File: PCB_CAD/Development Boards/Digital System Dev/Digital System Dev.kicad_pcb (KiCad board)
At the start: 6 copper layers, 100 x 100 mm, 189 parts, among them J1 STLINK, J10 F2_LOGIC, J101 Conn_01x04_Socket, J102 Conn_01x04_Socket, J103 Conn_01x04_Socket, J104 Conn_01x04_Socket, J13 F3_LOGIC, J15 DC_10V, J17 DISP0, J18 DISP1, J19 DISP2, J2 FADER_POW, J20 DISP3, J24 I2C_SEL_CLK, J25 I2C_SEL_SDA, J26 CV_SW_1, J27 CV_SW_2, J28 CV_SW_4, J29 CV_SW_3, J3 F0_LOGIC, J30 I2C, J31 CTRL_POW_SR, J4 FADER_POS, J5 LED_SEL, J6 F1_LOGIC, J7 SPI_MASTER, J8 EXT_POW_IN, Q1 2N7002, SW1 RESET, SW101 B2A, SW102 B2B, SW103 B2C, SW104 K1A, SW105 K1B, U1 STM32G474VETx, U101 74HCT595, U102 MCP23017x-x-SS, U28 74HC595, U29 74HC595, U30 74HC595, U31 74HC595, U32 74HC595, U33 74HC595, U34 74HC595, U35 74HC595, U36 74HC595, U37 74HC595, U38 74HC595, U39 74HC595, U4 TPS54302DDCT, U4 TPS5430DDA, U5 MCP4728, U6 TPS54302DDCT, U6 TPS5430DDA, X1 HSE_24

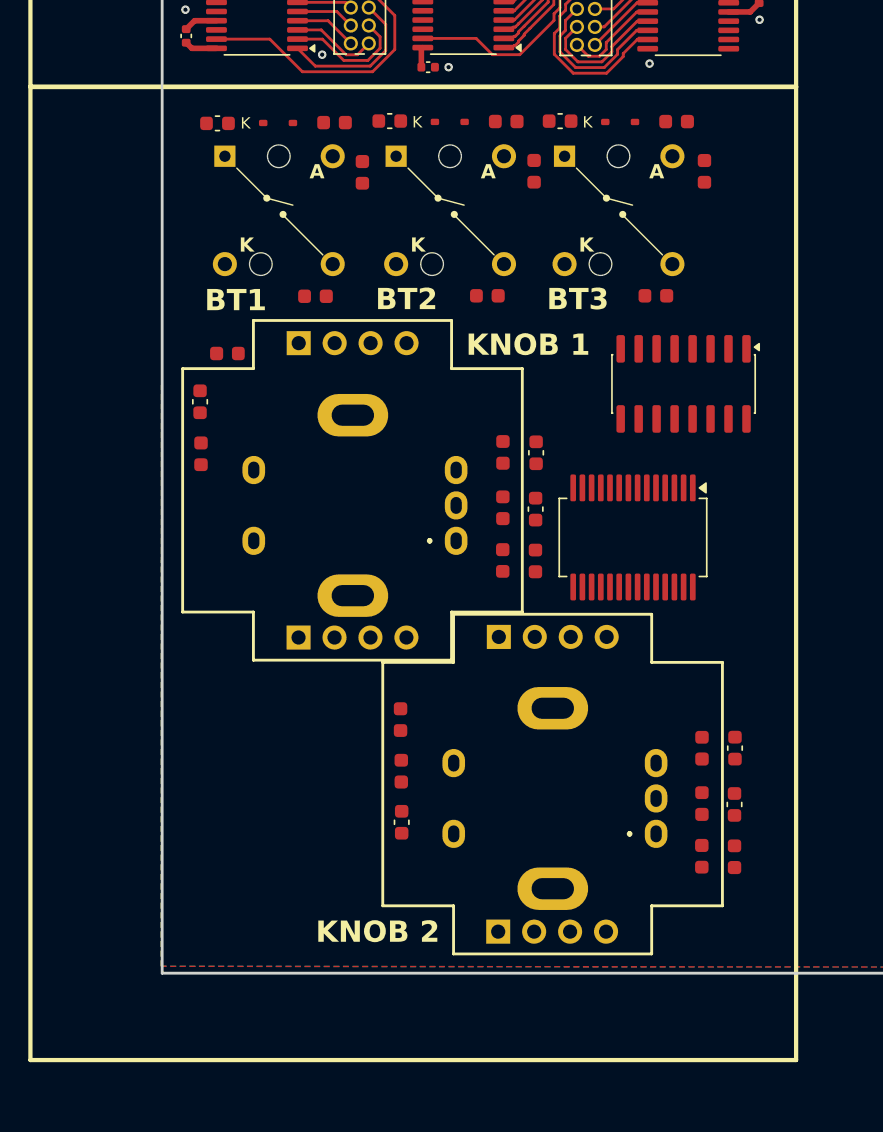
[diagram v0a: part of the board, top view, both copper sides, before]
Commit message: updates and input gain knob unsigned
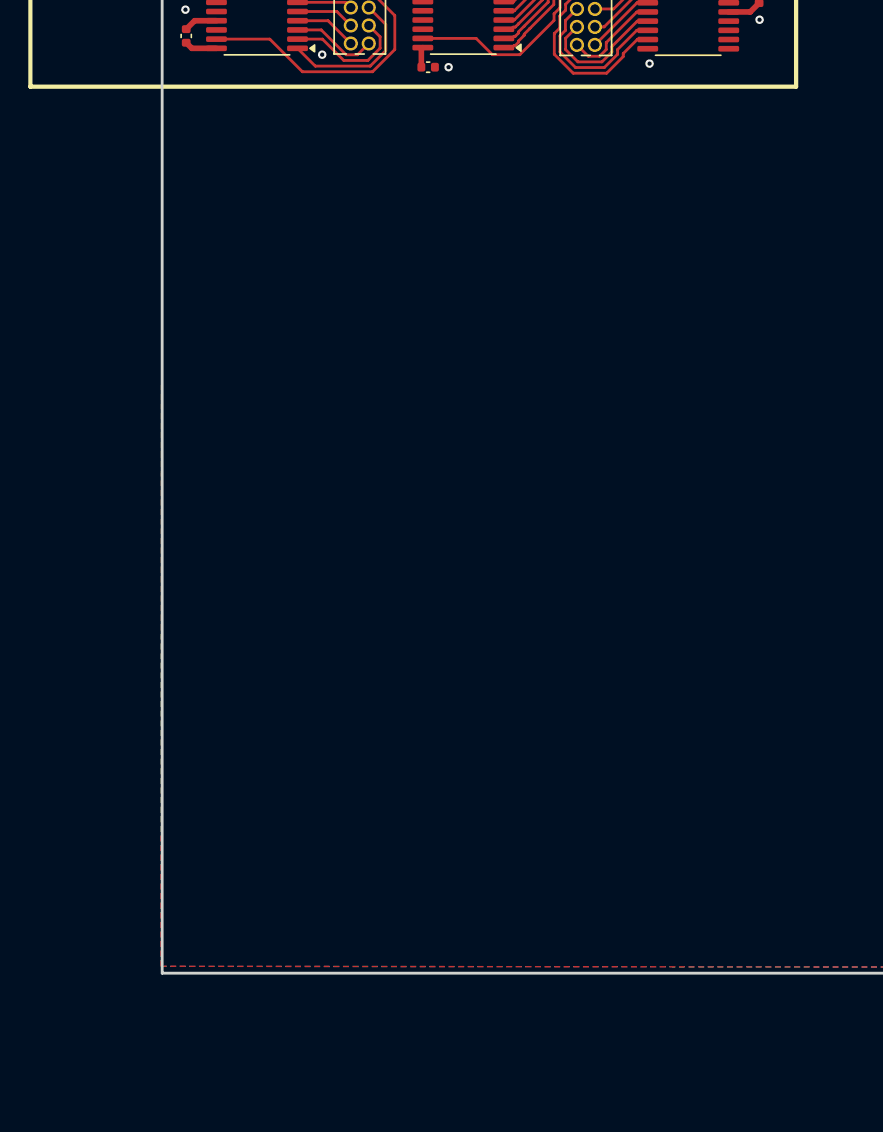
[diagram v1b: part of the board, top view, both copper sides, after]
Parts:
- removed C101, C102, C103: 1u, Capacitor_SMD:C_0603_1608Metric
- removed C104, C105, C106, C107, C108, C109: 10n, Capacitor_SMD:C_0603_1608Metric
- removed D101, D102, D103: 1N4148, Diode_SMD:D_SOD-323
- removed J101, J102, J103, J104: Conn_01x04_Socket, Connector_PinSocket_2.54mm:PinSocket_1x04_P2.54mm_Vertical
- removed R101, R102, R103: 47k, Resistor_SMD:R_0603_1608Metric
- removed R104, R105, R106: 15k, Resistor_SMD:R_0603_1608Metric
- removed R107, R108, R109: 330, Resistor_SMD:R_0603_1608Metric
- removed R110, R111, R112, R113, R114, R115: 10k, Resistor_SMD:R_0603_1608Metric
- removed R116, R117, R118, R119, R120, R121: 1k, Resistor_SMD:R_0603_1608Metric
- removed SW101: B2A, My Footprints:CFPB-1CC-4W6
- removed SW102: B2B, My Footprints:CFPB-1CC-4W6
- removed SW103: B2C, My Footprints:CFPB-1CC-4W6
- removed SW104: K1A, My Footprints:EC11J0924411
- removed SW105: K1B, My Footprints:EC11J0924411
- removed U101: 74HCT595, Package_SO:SOIC-16_3.9x9.9mm_P1.27mm
- removed U102: MCP23017x-x-SS, Package_SO:SSOP-28_5.3x10.2mm_P0.65mm
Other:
- board text removed: "BT1"
- board text removed: "BT2"
- board text removed: "BT3"
- board text removed: "KNOB 1"
- board text removed: "KNOB 2"

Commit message: pcb for displays
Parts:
- removed C17, C18, C21, C31, C33: 20p, Capacitor_SMD:C_0603_1608Metric
- removed C24, C27: 1u, Capacitor_SMD:C_0603_1608Metric
- removed C28, C32: 33u, Capacitor_SMD:CP_Elec_6.3x5.4
- removed C39: 100n, Capacitor_SMD:C_0402_1005Metric
- removed C40, C44, C45, C46, C53, C56, C58, C59: 100n, Capacitor_SMD:C_0603_1608Metric
- removed C51, C52, C54, C55, C57: 10u, Capacitor_SMD:C_1206_3216Metric
- removed D6: 2N5062, Package_TO_SOT_THT:TO-92
- removed DZ3: BZG04-12, PCM_4ms_Diode:D_DO-214AC_SMA
- removed J10: F2_LOGIC, Connector_PinHeader_2.54mm:PinHeader_1x04_P2.54mm_Vertical
- removed J13: F3_LOGIC, Connector_PinHeader_2.54mm:PinHeader_1x04_P2.54mm_Vertical
- removed J15: DC_10V, Connector_BarrelJack:BarrelJack_Horizontal
- removed J24: I2C_SEL_CLK, Connector_PinHeader_2.54mm:PinHeader_2x05_P2.54mm_Vertical
- removed J25: I2C_SEL_SDA, Connector_PinHeader_2.54mm:PinHeader_2x05_P2.54mm_Vertical
- removed J3: F0_LOGIC, Connector_PinHeader_2.54mm:PinHeader_1x04_P2.54mm_Vertical
- removed J30: I2C, Connector_PinHeader_1.27mm:PinHeader_2x08_P1.27mm_Vertical
- removed J31: CTRL_POW_SR, Connector_PinHeader_2.54mm:PinHeader_1x08_P2.54mm_Vertical
- removed J4: FADER_POS, Connector_PinHeader_2.54mm:PinHeader_1x04_P2.54mm_Vertical
- removed J5: LED_SEL, Connector_PinHeader_2.54mm:PinHeader_2x02_P2.54mm_Vertical
- removed J6: F1_LOGIC, Connector_PinHeader_2.54mm:PinHeader_1x04_P2.54mm_Vertical
- removed L1, L2: 6.8u, Inductor_SMD:L_1210_3225Metric
- removed R24: 12k, Resistor_SMD:R_0603_1608Metric
- removed R3: 22.1k, Resistor_SMD:R_0805_2012Metric
- removed R5: 13.5k, Resistor_SMD:R_0603_1608Metric
- removed U4, U6: TPS5430DDA, Package_SO:TI_SO-PowerPAD-8_ThermalVias
- removed U4, U6: TPS54302DDCT, Package_TO_SOT_SMD:SOT-23-6
- removed U5: MCP4728, Package_SO:MSOP-10_3x3mm_P0.5mm
- added C100: 100n, Capacitor_SMD:C_0603_1608Metric, B.Cu at (87.3, 136.7)
- added C101: 100n, Capacitor_SMD:C_0603_1608Metric, B.Cu at (88.8, 139.1)
- added C102: 100n, Capacitor_SMD:C_0603_1608Metric, B.Cu at (90.3, 136.7)
- added C103: 100n, Capacitor_SMD:C_0603_1608Metric, B.Cu at (91.9, 139.1)
- added C104: 100n, Capacitor_SMD:C_0603_1608Metric, B.Cu at (84.7, 146.7)
- added C105: 100n, Capacitor_SMD:C_0603_1608Metric, B.Cu at (86.0, 149.7)
- added C106: 100n, Capacitor_SMD:C_0603_1608Metric, B.Cu at (87.3, 146.7)
- added C107: 100n, Capacitor_SMD:C_0603_1608Metric, B.Cu at (88.5, 149.7)
- added C108: 100n, Capacitor_SMD:C_0603_1608Metric, B.Cu at (89.9, 146.6)
- added C109: 100n, Capacitor_SMD:C_0603_1608Metric, B.Cu at (91.4, 149.7)
- added C111: 100n, Capacitor_SMD:C_0603_1608Metric, B.Cu at (86.3, 120.1)
- added C112: 100n, Capacitor_SMD:C_0603_1608Metric, B.Cu at (87.6, 123.1)
- added C113: 100n, Capacitor_SMD:C_0603_1608Metric, B.Cu at (88.9, 120.1)
- added C114: 100n, Capacitor_SMD:C_0603_1608Metric, B.Cu at (90.1, 123.1)
- added C115: 100n, Capacitor_SMD:C_0603_1608Metric, B.Cu at (91.5, 120.1)
- added C116: 100n, Capacitor_SMD:C_0603_1608Metric, B.Cu at (84.4, 130.9)
- added C118: 100n, Capacitor_SMD:C_0603_1608Metric, B.Cu at (87.3, 130.9)
- added C119: 100n, Capacitor_SMD:C_0603_1608Metric, B.Cu at (88.8, 133.5)
- added C120: 100n, Capacitor_SMD:C_0603_1608Metric, B.Cu at (90.3, 130.9)
- added C121: 100n, Capacitor_SMD:C_0603_1608Metric, B.Cu at (91.8, 133.5)
- added C122: 100n, Capacitor_SMD:C_0603_1608Metric, B.Cu at (77.3, 123.1)
- added C124: 100n, Capacitor_SMD:C_0603_1608Metric, B.Cu at (79.9, 123.1)
- added C125: 100n, Capacitor_SMD:C_0603_1608Metric, B.Cu at (81.1, 120.1)
- added C126: 100n, Capacitor_SMD:C_0603_1608Metric, B.Cu at (82.3, 123.1)
- added C127: 100n, Capacitor_SMD:C_0603_1608Metric, B.Cu at (83.6, 120.1)
- added C128: 100n, Capacitor_SMD:C_0603_1608Metric, B.Cu at (75.4, 130.9)
- added C129: 100n, Capacitor_SMD:C_0603_1608Metric, B.Cu at (76.9, 133.5)
- added C130: 100n, Capacitor_SMD:C_0603_1608Metric, B.Cu at (78.4, 130.9)
- added C131: 100n, Capacitor_SMD:C_0603_1608Metric, B.Cu at (79.9, 133.5)
- added C132: 100n, Capacitor_SMD:C_0603_1608Metric, B.Cu at (81.4, 130.9)
- added C133: 100n, Capacitor_SMD:C_0603_1608Metric, B.Cu at (82.9, 133.5)
- added C134: 100n, Capacitor_SMD:C_0603_1608Metric, B.Cu at (75.3, 136.7)
- added C135: 100n, Capacitor_SMD:C_0603_1608Metric, B.Cu at (76.8, 139.1)
- added C136: 100n, Capacitor_SMD:C_0603_1608Metric, B.Cu at (78.3, 136.7)
- added C137: 100n, Capacitor_SMD:C_0603_1608Metric, B.Cu at (79.8, 139.1)
- added C138: 100n, Capacitor_SMD:C_0603_1608Metric, B.Cu at (81.3, 136.7)
- added C139: 100n, Capacitor_SMD:C_0603_1608Metric, B.Cu at (82.8, 139.1)
- added C140: 100n, Capacitor_SMD:C_0603_1608Metric, B.Cu at (77.2, 146.7)
- added C141: 100n, Capacitor_SMD:C_0603_1608Metric, B.Cu at (78.5, 149.7)
- added C142: 100n, Capacitor_SMD:C_0603_1608Metric, B.Cu at (79.7, 146.7)
- added C143: 100n, Capacitor_SMD:C_0603_1608Metric, B.Cu at (80.9, 149.7)
- added C144: 100n, Capacitor_SMD:C_0603_1608Metric, B.Cu at (82.3, 146.7)
- added C145: 100n, Capacitor_SMD:C_0603_1608Metric, B.Cu at (83.5, 149.7)
- added C146: 100n, Capacitor_SMD:C_0603_1608Metric, B.Cu at (95.6, 123.2)
- added C147: 100n, Capacitor_SMD:C_0603_1608Metric, B.Cu at (96.8, 120.1)
- added C148: 100n, Capacitor_SMD:C_0603_1608Metric, B.Cu at (98.1, 123.2)
- added C149: 100n, Capacitor_SMD:C_0603_1608Metric, B.Cu at (99.4, 120.2)
- added C150: 100n, Capacitor_SMD:C_0603_1608Metric, B.Cu at (101.0, 123.2)
- added C151: 100n, Capacitor_SMD:C_0603_1608Metric, B.Cu at (102.3, 120.2)
- added C152: 100n, Capacitor_SMD:C_0603_1608Metric, B.Cu at (95.6, 130.8)
- added C153: 100n, Capacitor_SMD:C_0603_1608Metric, B.Cu at (97.1, 133.1)
- added C154: 100n, Capacitor_SMD:C_0603_1608Metric, B.Cu at (98.6, 130.8)
- added C155: 100n, Capacitor_SMD:C_0603_1608Metric, B.Cu at (100.1, 133.1)
- added C156: 100n, Capacitor_SMD:C_0603_1608Metric, B.Cu at (101.6, 130.8)
- added C157: 100n, Capacitor_SMD:C_0603_1608Metric, B.Cu at (103.1, 133.1)
- added C158: 100n, Capacitor_SMD:C_0603_1608Metric, B.Cu at (95.6, 149.9)
- added C159: 100n, Capacitor_SMD:C_0603_1608Metric, B.Cu at (97.1, 146.8)
- added C160: 100n, Capacitor_SMD:C_0603_1608Metric, B.Cu at (98.4, 149.9)
- added C161: 100n, Capacitor_SMD:C_0603_1608Metric, B.Cu at (99.6, 146.8)
- added C162: 100n, Capacitor_SMD:C_0603_1608Metric, B.Cu at (100.8, 149.9)
- added C163: 100n, Capacitor_SMD:C_0603_1608Metric, B.Cu at (102.0, 146.8)
- added C164: 100n, Capacitor_SMD:C_0603_1608Metric, B.Cu at (95.6, 136.8)
- added C165: 100n, Capacitor_SMD:C_0603_1608Metric, B.Cu at (97.1, 139.2)
- added C166: 100n, Capacitor_SMD:C_0603_1608Metric, B.Cu at (98.6, 136.8)
- added C167: 100n, Capacitor_SMD:C_0603_1608Metric, B.Cu at (100.1, 139.2)
- added C168: 100n, Capacitor_SMD:C_0603_1608Metric, B.Cu at (101.6, 136.8)
- added C169: 100n, Capacitor_SMD:C_0603_1608Metric, B.Cu at (103.1, 139.2)
- added C170: 100n, Capacitor_SMD:C_0603_1608Metric, F.Cu at (83.6, 113.9)
- added C171: 100n, Capacitor_SMD:C_0603_1608Metric, F.Cu at (104.2, 134.5)
- added C172: 100n, Capacitor_SMD:C_0603_1608Metric, F.Cu at (104.2, 138.2)
- added C173: 100n, Capacitor_SMD:C_0603_1608Metric, F.Cu at (109.5, 114.0)
- added C174: 100n, Capacitor_SMD:C_0603_1608Metric, F.Cu at (102.0, 113.8)
- added C175: 100n, Capacitor_SMD:C_0603_1608Metric, F.Cu at (80.4, 156.0)
- added C176: 100n, Capacitor_SMD:C_0603_1608Metric, F.Cu at (85.7, 138.1)
- added C177: 100n, Capacitor_SMD:C_0603_1608Metric, F.Cu at (85.7, 134.4)
- added C178: 100n, Capacitor_SMD:C_0603_1608Metric, F.Cu at (91.0, 114.0)
- added C179: 100n, Capacitor_SMD:C_0603_1608Metric, F.Cu at (87.8, 155.9)
- added C180: 100n, Capacitor_SMD:C_0603_1608Metric, F.Cu at (98.7, 156.0)
- added C181: 100n, Capacitor_SMD:C_0603_1608Metric, F.Cu at (106.1, 156.0)
- added C74: 100n, Capacitor_SMD:C_0603_1608Metric, B.Cu at (103.3, 149.9)
- added C75: 100n, Capacitor_SMD:C_0603_1608Metric, B.Cu at (104.5, 146.7)
- added C76: 100n, Capacitor_SMD:C_0603_1608Metric, B.Cu at (105.7, 149.9)
- added C77: 100n, Capacitor_SMD:C_0603_1608Metric, B.Cu at (107.1, 146.8)
- added C78: 100n, Capacitor_SMD:C_0603_1608Metric, B.Cu at (108.3, 149.8)
- added C79: 100n, Capacitor_SMD:C_0603_1608Metric, B.Cu at (109.7, 146.8)
- added C80: 100n, Capacitor_SMD:C_0603_1608Metric, B.Cu at (112.1, 139.2)
- added C81: 100n, Capacitor_SMD:C_0603_1608Metric, B.Cu at (110.6, 137.0)
- added C82: 100n, Capacitor_SMD:C_0603_1608Metric, B.Cu at (109.1, 139.2)
- added C83: 100n, Capacitor_SMD:C_0603_1608Metric, B.Cu at (107.6, 136.9)
- added C84: 100n, Capacitor_SMD:C_0603_1608Metric, B.Cu at (106.1, 139.2)
- added C85: 100n, Capacitor_SMD:C_0603_1608Metric, B.Cu at (104.6, 136.8)
- added C86: 100n, Capacitor_SMD:C_0603_1608Metric, B.Cu at (103.5, 123.2)
- added C87: 100n, Capacitor_SMD:C_0603_1608Metric, B.Cu at (104.7, 120.2)
- added C88: 100n, Capacitor_SMD:C_0603_1608Metric, B.Cu at (106.0, 123.2)
- added C89: 100n, Capacitor_SMD:C_0603_1608Metric, B.Cu at (107.2, 120.2)
- added C90: 100n, Capacitor_SMD:C_0603_1608Metric, B.Cu at (108.5, 123.2)
- added C91: 100n, Capacitor_SMD:C_0603_1608Metric, B.Cu at (109.8, 120.2)
- added C92: 100n, Capacitor_SMD:C_0603_1608Metric, B.Cu at (104.6, 130.8)
- added C93: 100n, Capacitor_SMD:C_0603_1608Metric, B.Cu at (106.1, 133.1)
- added C94: 100n, Capacitor_SMD:C_0603_1608Metric, B.Cu at (107.6, 130.8)
- added C95: 100n, Capacitor_SMD:C_0603_1608Metric, B.Cu at (109.1, 133.1)
- added C96: 100n, Capacitor_SMD:C_0603_1608Metric, B.Cu at (110.6, 130.8)
- added C97: 100n, Capacitor_SMD:C_0603_1608Metric, B.Cu at (112.1, 133.0)
- added C98: 100n, Capacitor_SMD:C_0603_1608Metric, B.Cu at (84.3, 136.7)
- added C99: 100n, Capacitor_SMD:C_0603_1608Metric, B.Cu at (85.8, 139.1)
- added H1: MountingScrew, MountingHole:MountingHole_3.2mm_M3, F.Cu at (75.0, 117.0)
- added H2: MountingScrew, MountingHole:MountingHole_3.2mm_M3, F.Cu at (163.0, 117.0)
- added H3: MountingScrew, MountingHole:MountingHole_3.2mm_M3, F.Cu at (75.0, 182.0)
- added H4: MountingScrew, MountingHole:MountingHole_3.2mm_M3, F.Cu at (163.0, 182.0)
- added R10: 1.5k, Resistor_SMD:R_0603_1608Metric, F.Cu at (167.5, 149.7)
- added R11: 1.5k, Resistor_SMD:R_0603_1608Metric, F.Cu at (160.3, 148.2)
- added R12: 1.5k, Resistor_SMD:R_0603_1608Metric, F.Cu at (160.3, 151.7)
- added R13: 1.5k, Resistor_SMD:R_0603_1608Metric, F.Cu at (160.3, 146.4)
- added R14: 1.5k, Resistor_SMD:R_0603_1608Metric, F.Cu at (160.3, 144.7)
- added R2: 10k, Resistor_SMD:R_0603_1608Metric, F.Cu at (157.8, 154.0)
- added R7: 1.5k, Resistor_SMD:R_0603_1608Metric, F.Cu at (160.3, 153.4)
- added R8: 1.5k, Resistor_SMD:R_0603_1608Metric, F.Cu at (160.3, 149.9)
- added R9: 1.5k, Resistor_SMD:R_0603_1608Metric, F.Cu at (167.5, 153.4)
- added REF**: LayerMarker_6_8.89x2.54mm_TextH1mm_P1.27mm, Symbol:LayerMarker_6_8.89x2.54mm_TextH1mm_P1.27mm, F.Cu at (159.0, 176.8)
- C110, C117, C123: moved to B.Cu
- C16: value 20p -> 100n
- C48: value 100n -> 10u; footprint Capacitor_SMD:C_0603_1608Metric -> Capacitor_SMD:C_1206_3216Metric
- C62, C63, C64, C65, C66, C67, C68, C69, C70, C71, C72, C73: footprint Capacitor_SMD:C_0402_1005Metric -> Capacitor_SMD:C_0603_1608Metric
- J2: value FADER_POW -> FADER; footprint Connector_PinHeader_2.54mm:PinHeader_1x04_P2.54mm_Vertical -> Connector_PinHeader_1.27mm:PinHeader_2x12_P1.27mm_Vertical
- R23: value 1k -> 680
- moved J7 217.1 mm to (165.3, 168.2), turned to -90 degrees
- moved SP1 189.2 mm to (159.3, 159.0), turned to 180 degrees
- moved J2 167.9 mm to (117.4, 128.5)
- moved C117 166.7 mm to (85.8, 133.5), turned to -90 degrees
- moved SW1 165.1 mm to (147.3, 124.0), turned to 90 degrees
- moved C42 163.6 mm to (94.8, 114.5), turned to 180 degrees
- moved DZ1 163.2 mm to (118.7, 122.6)
- moved R1 162.2 mm to (152.3, 136.5), turned to -135 degrees
- moved C110 161.5 mm to (85.0, 123.1), turned to 90 degrees
- moved C123 160.7 mm to (78.5, 120.1), turned to 90 degrees
- moved C41 157.5 mm to (95.0, 155.4)
- moved R18 156.6 mm to (82.3, 180.4), turned to 180 degrees
- moved D4 154.0 mm to (118.7, 118.2), turned to 180 degrees
- moved C7 139.3 mm to (135.8, 136.0), turned to 135 degrees
- moved R19 139.2 mm to (101.5, 180.4), turned to 180 degrees
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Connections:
- C110 pad 1: +5V -> /cv_sw/1_14
- C117 pad 1: +3V3 -> /cv_sw/1_9
- C123 pad 1: +3V3 -> /cv_sw/1_4
- C16 pad 1: +3V3 -> Net-(SP1-A)
- C16 pad 2: Net-(U4-FB) -> GND
- J17 pad 10: unconnected-(J17-Pin_10-Pad10) -> DISP_D4_FMC
- J17 pad 11: unconnected-(J17-Pin_11-Pad11) -> DISP_D3_FMC
- J17 pad 12: unconnected-(J17-Pin_12-Pad12) -> DISP_D2_FMC
- J17 pad 13: unconnected-(J17-Pin_13-Pad13) -> DISP_D1_FMC
- J17 pad 14: unconnected-(J17-Pin_14-Pad14) -> DISP_D0_FMC
- J17 pad 15: unconnected-(J17-Pin_15-Pad15) -> DISP_NOE_FMC
- J17 pad 16: unconnected-(J17-Pin_16-Pad16) -> DISP_NWE_FMC
- J17 pad 17: unconnected-(J17-Pin_17-Pad17) -> DISP_A0_FMC
- J17 pad 18: unconnected-(J17-Pin_18-Pad18) -> DISP_CS0
- J17 pad 19: unconnected-(J17-Pin_19-Pad19) -> xTE0
- J17 pad 20: +3V3 -> DISP_RST
- J17 pad 21: unconnected-(J17-Pin_21-Pad21) -> GND
- J17 pad 3: +3V3 -> GND
- J17 pad 4: +3V3 -> GND
- J17 pad 5: unconnected-(J17-Pin_5-Pad5) -> GND
- J17 pad 7: unconnected-(J17-Pin_7-Pad7) -> DISP_D7_FMC
- J17 pad 8: unconnected-(J17-Pin_8-Pad8) -> DISP_D6_FMC
- J17 pad 9: unconnected-(J17-Pin_9-Pad9) -> DISP_D5_FMC
- J18 pad 10: unconnected-(J18-Pin_10-Pad10) -> DISP_D4_FMC
- J18 pad 11: unconnected-(J18-Pin_11-Pad11) -> DISP_D3_FMC
- J18 pad 12: unconnected-(J18-Pin_12-Pad12) -> DISP_D2_FMC
- J18 pad 13: unconnected-(J18-Pin_13-Pad13) -> DISP_D1_FMC
- J18 pad 14: unconnected-(J18-Pin_14-Pad14) -> DISP_D0_FMC
- J18 pad 15: unconnected-(J18-Pin_15-Pad15) -> DISP_NOE_FMC
- J18 pad 16: unconnected-(J18-Pin_16-Pad16) -> DISP_NWE_FMC
- J18 pad 17: unconnected-(J18-Pin_17-Pad17) -> DISP_A0_FMC
- J18 pad 18: unconnected-(J18-Pin_18-Pad18) -> DISP_CS1
- J18 pad 19: unconnected-(J18-Pin_19-Pad19) -> xTE1
- J18 pad 20: +3V3 -> DISP_RST
- J18 pad 21: unconnected-(J18-Pin_21-Pad21) -> GND
- J18 pad 3: Net-(J18-Pin_3) -> GND
- J18 pad 4: Net-(J18-Pin_3) -> GND
- J18 pad 5: unconnected-(J18-Pin_5-Pad5) -> GND
- J18 pad 7: unconnected-(J18-Pin_7-Pad7) -> DISP_D7_FMC
- J18 pad 8: unconnected-(J18-Pin_8-Pad8) -> DISP_D6_FMC
- J18 pad 9: unconnected-(J18-Pin_9-Pad9) -> DISP_D5_FMC
- J19 pad 10: unconnected-(J19-Pin_10-Pad10) -> DISP_D4_FMC
- J19 pad 11: unconnected-(J19-Pin_11-Pad11) -> DISP_D3_FMC
- J19 pad 12: unconnected-(J19-Pin_12-Pad12) -> DISP_D2_FMC
- J19 pad 13: unconnected-(J19-Pin_13-Pad13) -> DISP_D1_FMC
- J19 pad 14: unconnected-(J19-Pin_14-Pad14) -> DISP_D0_FMC
- J19 pad 15: unconnected-(J19-Pin_15-Pad15) -> DISP_NOE_FMC
- J19 pad 16: unconnected-(J19-Pin_16-Pad16) -> DISP_NWE_FMC
- J19 pad 17: unconnected-(J19-Pin_17-Pad17) -> DISP_A0_FMC
- J19 pad 18: unconnected-(J19-Pin_18-Pad18) -> DISP_CS2
- J19 pad 19: unconnected-(J19-Pin_19-Pad19) -> xTE2
- J19 pad 20: +3V3 -> DISP_RST
- J19 pad 21: unconnected-(J19-Pin_21-Pad21) -> GND
- J19 pad 3: +3V3 -> GND
- J19 pad 4: +3V3 -> GND
- J19 pad 5: unconnected-(J19-Pin_5-Pad5) -> GND
- J19 pad 7: unconnected-(J19-Pin_7-Pad7) -> DISP_D7_FMC
- J19 pad 8: unconnected-(J19-Pin_8-Pad8) -> DISP_D6_FMC
- J19 pad 9: unconnected-(J19-Pin_9-Pad9) -> DISP_D5_FMC
- J2 pad 1: +10V -> F0_MoB
- J2 pad 2: GND -> F2_MoB
- J2 pad 3: +5V -> F3_MoB
- J2 pad 4: GND -> F0_MoA
- J20 pad 10: unconnected-(J20-Pin_10-Pad10) -> DISP_D4_FMC
- J20 pad 11: unconnected-(J20-Pin_11-Pad11) -> DISP_D3_FMC
- J20 pad 12: unconnected-(J20-Pin_12-Pad12) -> DISP_D2_FMC
- J20 pad 13: unconnected-(J20-Pin_13-Pad13) -> DISP_D1_FMC
- J20 pad 14: unconnected-(J20-Pin_14-Pad14) -> DISP_D0_FMC
- J20 pad 15: unconnected-(J20-Pin_15-Pad15) -> DISP_NOE_FMC
- J20 pad 16: unconnected-(J20-Pin_16-Pad16) -> DISP_NWE_FMC
- J20 pad 17: unconnected-(J20-Pin_17-Pad17) -> DISP_A0_FMC
- J20 pad 18: unconnected-(J20-Pin_18-Pad18) -> DISP_CS3
- J20 pad 19: unconnected-(J20-Pin_19-Pad19) -> xTE3
- J20 pad 20: +3V3 -> DISP_RST
- J20 pad 21: unconnected-(J20-Pin_21-Pad21) -> GND
- J20 pad 3: +3V3 -> GND
- J20 pad 4: +3V3 -> GND
- J20 pad 5: unconnected-(J20-Pin_5-Pad5) -> GND
- J20 pad 7: unconnected-(J20-Pin_7-Pad7) -> DISP_D7_FMC
- J20 pad 8: unconnected-(J20-Pin_8-Pad8) -> DISP_D6_FMC
- J20 pad 9: unconnected-(J20-Pin_9-Pad9) -> DISP_D5_FMC
- J7 pad 2: MASTER_Clock -> MASTER_MISO
- J7 pad 3: MASTER_MOSI -> MASTER_Clock
- J7 pad 4: MASTER_MISO -> MASTER_CS_IN
- J7 pad 5: MASTER_CS_IN -> MASTER_MOSI
- J8 pad 3: +10V -> GND
- R23 pad 1: Net-(D6-G) -> LED_TEST
- R23 pad 2: GND -> Net-(D3-A)
- SP1 pad 1: GND -> Net-(SP1-A)
- TP11 pad 1: +10V -> Net-(U1-PF0)
- U1 pad 1: unconnected-(U1-PE2-Pad1) -> xPE2
- U1 pad 10: unconnected-(U1-PF9-Pad10) -> xPF9
- U1 pad 19: unconnected-(U1-PF2-Pad19) -> LED_TEST
- U1 pad 2: unconnected-(U1-PE3-Pad2) -> xPE3
- U1 pad 3: unconnected-(U1-PE4-Pad3) -> DISP_RST
- U1 pad 43: unconnected-(U1-PE12-Pad43) -> xPE12
- U1 pad 5: unconnected-(U1-PE6-Pad5) -> xPE6
- U1 pad 55: unconnected-(U1-PD8-Pad55) -> xPD8
- U1 pad 68: unconnected-(U1-PC9-Pad68) -> xPC9
- U1 pad 7: unconnected-(U1-PC13-Pad7) -> xPC13
- U1 pad 8: unconnected-(U1-PC14-Pad8) -> xPC14
- U1 pad 9: unconnected-(U1-PC15-Pad9) -> xPC15
- U1 pad 94: unconnected-(U1-PB7-Pad94) -> xPB7
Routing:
- net +3V3: track 24.4 -> 214.8 mm, vias 0 -> 35
- net DISP_D0_FMC: track 0.00 -> 159.6 mm, vias 0 -> 5
- net DISP_D1_FMC: track 0.00 -> 156.9 mm, vias 0 -> 5
- net SHIFTREG_Latch: track 0.00 -> 154.5 mm, vias 0 -> 12
- net DISP_D4_FMC: track 0.00 -> 152.8 mm, vias 0 -> 5
- net DISP_D5_FMC: track 0.00 -> 150.2 mm, vias 0 -> 5
- net DISP_D3_FMC: track 0.00 -> 147.2 mm, vias 0 -> 5
- net DISP_D6_FMC: track 0.00 -> 146.9 mm, vias 0 -> 5
- net DISP_D2_FMC: track 0.00 -> 146.4 mm, vias 0 -> 5
- net DISP_D7_FMC: track 0.00 -> 144.7 mm, vias 0 -> 5
- net GND: track 19.2 -> 140.6 mm, vias 34 -> 53
- net SHIFTREG_Clock: track 0.00 -> 113.3 mm, vias 0 -> 11
- net Net-(U30-QH'): track 0.00 -> 50.9 mm, vias 0 -> 2
- net Net-(U30-SER): track 0.00 -> 47.0 mm, vias 0 -> 2
- net MASTER_MOSI: track 0.00 -> 39.2 mm, vias 0 -> 1
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- added copper zone on In2.Cu, net +3V3
- added copper zone on In2.Cu, net +5V
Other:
- board size 100 x 100 mm -> 100 x 76.8 mm
- board text added: "DISP 0"
- board text added: "DISP 1"
- board text added: "DISP 2"
- board text added: "DISP 3"
- board text added: "LOGIC CVs"
- board text added: "SPI MASTER"
- board text added: "ST-LINK"
- board text removed: "SWITCH CVs"

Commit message: digital dev (or maybe final) board
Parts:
- removed C100, C101, C102, C103, C104, C105, C106, C107, C108, C109, C110, C111, C112, C113, C114, C115, C116, C117, C118, C119, C120, C121, C122, C123, C124, C125, C126, C127, C128, C129, C130, C131, C132, C133, C134, C135, C136, C137, C138, C139, C140, C141, C142, C143, C144, C145, C146, C147, C148, C149, C150, C151, C152, C153, C154, C155, C156, C157, C158, C159, C16, C160, C161, C162, C163, C164, C165, C166, C167, C168, C169, C170, C171, C172, C173, C174, C175, C176, C177, C178, C179, C180, C181, C65, C66, C67, C68, C69, C70, C71, C72, C73, C74, C75, C76, C77, C78, C79, C80, C81, C82, C83, C84, C85, C86, C87, C88, C89, C90, C91, C92, C93, C94, C95, C96, C97, C98, C99: 100n, Capacitor_SMD:C_0603_1608Metric
- removed C41, C42: 10u, Capacitor_SMD:C_1206_3216Metric
- removed J26: CV_SW_1, Connector_PinHeader_1.27mm:PinHeader_2x12_P1.27mm_Vertical
- removed J27: CV_SW_2, Connector_PinHeader_1.27mm:PinHeader_2x12_P1.27mm_Vertical
- removed J28: CV_SW_4, Connector_PinHeader_1.27mm:PinHeader_2x12_P1.27mm_Vertical
- removed J29: CV_SW_3, Connector_PinHeader_1.27mm:PinHeader_2x12_P1.27mm_Vertical
- removed J8: EXT_POW_IN, Connector_PinHeader_2.54mm:PinHeader_1x04_P2.54mm_Vertical
- removed R2: 10k, Resistor_SMD:R_0603_1608Metric
- removed the REF** at (159.0, 176.8)
- removed SP1: BOOT_MODE, Jumper:SolderJumper-3_P2.0mm_Open_TrianglePad1.0x1.5mm
- removed TP10, TP11, TP19, TP9: TestPoint_Probe, TestPoint:TestPoint_Keystone_5019_Miniature
- removed U28, U29, U30, U31, U32, U33, U34, U35, U36, U37, U38, U39: 74HC595, Package_SO:TSSOP-16_4.4x5mm_P0.65mm
- added C30: 100n, Capacitor_SMD:C_0603_1608Metric, F.Cu at (113.6, 115.6)
- added C31: 100n, Capacitor_SMD:C_0603_1608Metric, F.Cu at (103.5, 127.6)
- added C32: 100n, Capacitor_SMD:C_0603_1608Metric, F.Cu at (134.0, 118.2)
- added J10: 10V, Connector_PinSocket_2.54mm:PinSocket_1x05_P2.54mm_Vertical, F.Cu at (132.1, 113.4)
- added J3: 3V3, Connector_PinSocket_2.54mm:PinSocket_1x05_P2.54mm_Vertical, F.Cu at (91.4, 113.3)
- added J4: 5V, Connector_PinSocket_2.54mm:PinSocket_1x05_P2.54mm_Vertical, F.Cu at (116.5, 113.4)
- added J5: GND, Connector_PinSocket_2.54mm:PinSocket_1x05_P2.54mm_Vertical, F.Cu at (157.7, 114.3)
- added J6: PINS_LEFT, Connector_PinHeader_2.54mm:PinHeader_2x18_P2.54mm_Vertical, F.Cu at (158.2, 130.8)
- added J9: DC_IN, Connector_BarrelJack:BarrelJack_Horizontal, F.Cu at (84.5, 124.9)
- added JP1: SolderJumper_2_Open, Jumper:SolderJumper-2_P1.3mm_Open_TrianglePad1.0x1.5mm, F.Cu at (167.0, 176.8)
- added JP2: SolderJumper_2_Open, Jumper:SolderJumper-2_P1.3mm_Open_TrianglePad1.0x1.5mm, F.Cu at (167.2, 160.4)
- added JP3: SolderJumper_2_Open, Jumper:SolderJumper-2_P1.3mm_Open_TrianglePad1.0x1.5mm, F.Cu at (91.9, 172.6)
- added JP4: SolderJumper_2_Open, Jumper:SolderJumper-2_P1.3mm_Open_TrianglePad1.0x1.5mm, F.Cu at (91.9, 170.1)
- added JP5: SolderJumper_2_Open, Jumper:SolderJumper-2_P1.3mm_Open_TrianglePad1.0x1.5mm, F.Cu at (91.9, 165.0)
- added JP6: SolderJumper_2_Open, Jumper:SolderJumper-2_P1.3mm_Open_TrianglePad1.0x1.5mm, F.Cu at (91.9, 167.5)
- added JP7: SolderJumper_2_Open, Jumper:SolderJumper-2_P1.3mm_Open_TrianglePad1.0x1.5mm, F.Cu at (91.9, 160.0)
- added JP8: SolderJumper_2_Open, Jumper:SolderJumper-2_P1.3mm_Open_TrianglePad1.0x1.5mm, F.Cu at (91.9, 162.5)
- added REF**: LayerMarker_6_8.89x2.54mm_TextH1mm_P1.27mm_BottomMirrored, Symbol:LayerMarker_6_8.89x2.54mm_TextH1mm_P1.27mm_BottomMirrored, F.Cu at (170.0, 122.2)
- added U2: DFR0570, My Footprints:DFR05xx_DC-DC, B.Cu at (102.0, 126.0)
- added U3: DFR0571, My Footprints:DFR05xx_DC-DC, B.Cu at (130.4, 126.0)
- C62, C63, C64: value 100n -> 10u; footprint Capacitor_SMD:C_0603_1608Metric -> Capacitor_SMD:CP_Elec_6.3x5.8
- J2: value FADER -> PINS_LEFT; footprint Connector_PinHeader_1.27mm:PinHeader_2x12_P1.27mm_Vertical -> Connector_PinHeader_2.54mm:PinHeader_2x18_P2.54mm_Vertical
- J7: value SPI_MASTER -> DISP; footprint Connector_PinHeader_2.54mm:PinHeader_1x06_P2.54mm_Vertical -> Connector_PinHeader_2.54mm:PinHeader_2x06_P2.54mm_Vertical
- moved J1 87.2 mm to (118.2, 123.7)
- moved R10 81.9 mm to (88.1, 170.0), turned to 180 degrees
- moved R9 81.7 mm to (88.1, 172.6), turned to 180 degrees
- moved R14 74.4 mm to (88.0, 162.5), turned to 180 degrees
- moved R11 74.1 mm to (88.1, 165.0), turned to 180 degrees
- moved R12 73.9 mm to (88.1, 167.5), turned to 180 degrees
- moved R13 73.5 mm to (88.0, 160.0), turned to 180 degrees
- moved J2 41.5 mm to (76.0, 131.0)
- moved J7 40.9 mm to (124.6, 171.6), turned to 135 degrees
- moved C10 32.3 mm to (123.8, 138.0)
- moved D4 30.2 mm to (148.8, 115.6)
- moved DZ1 30.2 mm to (148.8, 120.1)
- moved R22 30.2 mm to (151.8, 116.1)
- moved C22 30.2 mm to (153.7, 116.1)
- moved C64 29.5 mm to (128.0, 120.5), turned to 90 degrees
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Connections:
- C62 pad 1: +3V3 -> +10V
- C64 pad 1: +3V3 -> +5V
- J17 pad 19: xTE0 -> unconnected-(J17-Pin_19-Pad19)
- J18 pad 19: xTE1 -> unconnected-(J18-Pin_19-Pad19)
- J19 pad 19: xTE2 -> unconnected-(J19-Pin_19-Pad19)
- J2 pad 1: F0_MoB -> F2_MoB
- J2 pad 10: F3_ADC -> DISP_CS3
- J2 pad 11: GND -> DISP_CS2
- J2 pad 12: F0_ADC -> DISP_CS1
- J2 pad 13: GND -> DISP_CS0
- J2 pad 14: F1_MoA -> F3_Touch
- J2 pad 15: +3V3 -> F1_MoA
- J2 pad 16: F1_ADC -> F1_MoB
- J2 pad 17: GND -> COMP_ADC0
- J2 pad 18: F2_ADC -> LED_Clock
- J2 pad 19: GND -> LED_Latch
- J2 pad 2: F2_MoB -> F0_MoA
- J2 pad 20: F1_MoB -> LED_Data
- J2 pad 21: F1_Touch -> COMP_ADC3
- J2 pad 22: unconnected-(J2-Pin_22-Pad22) -> COMP_CV0
- J2 pad 23: unconnected-(J2-Pin_23-Pad23) -> COMP_ADC1
- J2 pad 24: unconnected-(J2-Pin_24-Pad24) -> COMP_CV2
- J2 pad 3: F3_MoB -> F2_MoA
- J2 pad 4: F0_MoA -> xPA7
- J2 pad 5: GND -> F0_ADC
- J2 pad 6: F2_MoA -> F1_Touch
- J2 pad 7: +5V -> COMP_CV1
- J2 pad 8: F3_MoA -> F3_MoB
- J2 pad 9: GND -> F2_Touch
- J20 pad 19: xTE3 -> unconnected-(J20-Pin_19-Pad19)
- J7 pad 1: +3V3 -> DISP_D7_FMC
- J7 pad 2: MASTER_MISO -> DISP_D6_FMC
- J7 pad 3: MASTER_Clock -> DISP_D5_FMC
- J7 pad 4: MASTER_CS_IN -> DISP_D4_FMC
- J7 pad 5: MASTER_MOSI -> DISP_D3_FMC
- J7 pad 6: GND -> DISP_D2_FMC
- R10 pad 1: +3V3 -> Net-(JP4-A)
- R11 pad 1: +3V3 -> Net-(JP5-A)
- R12 pad 1: +3V3 -> Net-(JP6-A)
- R13 pad 1: +3V3 -> Net-(JP7-A)
- R14 pad 1: +3V3 -> Net-(JP8-A)
- R7 pad 1: +3V3 -> Net-(JP1-A)
- R8 pad 1: +3V3 -> Net-(JP2-A)
- R9 pad 1: +3V3 -> Net-(JP3-A)
- U1 pad 15: MASTER_CS_IN -> F1_ADC
- U1 pad 17: DISP_PWM -> F2_ADC
- U1 pad 18: COMP_ADC0 -> F3_ADC
- U1 pad 29: MASTER_MOSI -> xPA7
- U1 pad 3: DISP_RST -> F3_MoA
- U1 pad 30: COMP_ADC2 -> F0_ADC
- U1 pad 31: COMP_ADC3 -> F1_Touch
- U1 pad 32: F3_MoA -> COMP_CV1
- U1 pad 33: COMP_ADC1 -> F3_MoB
- U1 pad 34: DISP_CS0 -> F2_Touch
- U1 pad 4: F3_MoB -> F0_Touch
- U1 pad 42: F3_ADC -> DISP_CS3
- U1 pad 43: xPE12 -> DISP_CS2
- U1 pad 44: F0_ADC -> DISP_CS1
- U1 pad 45: DISP_CS1 -> DISP_CS0
- U1 pad 46: DISP_CS2 -> F3_Touch
- U1 pad 50: LED_Data -> F1_MoB
- U1 pad 51: LED_Clock -> COMP_ADC0
- U1 pad 52: COMP_CV1 -> LED_Clock
- U1 pad 54: DISP_CS3 -> LED_Data
- U1 pad 55: xPD8 -> COMP_ADC3
- U1 pad 57: F1_ADC -> COMP_ADC1
- U1 pad 60: F2_ADC -> COMP_ADC2
- U1 pad 68: xPC9 -> I2C3_Data
- U1 pad 7: xPC13 -> DISP_RST
- U1 pad 71: F1_MoB -> DISP_PWM
- U1 pad 79: F3_Touch -> DAC_LDAC4
- U1 pad 80: F2_Touch -> DAC_LDAC3
- U1 pad 81: F1_Touch -> DAC_LDAC2
- U1 pad 84: F0_Touch -> DAC_LDAC0
- U1 pad 85: DAC_LDAC4 -> xPD3
- U1 pad 88: DAC_LDAC3 -> DAC_LDAC1
- U1 pad 92: I2C3_Data -> MASTER_MOSI
- U1 pad 93: DAC_LDAC2 -> MASTER_CS_IN
- U1 pad 95: Net-(U1-PB8) -> GND
- U1 pad 97: DAC_LDAC1 -> xPE0
- U1 pad 98: DAC_LDAC0 -> xPE1
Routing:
- net SHIFTREG_Latch: track 154.5 -> 41.0 mm, vias 12 -> 0
- net +10V: track 0.00 -> 106.1 mm, vias 0 -> 1
- net DISP_D5_FMC: track 150.2 -> 46.8 mm, vias 5 -> 2
- net +5V: track 18.3 -> 117.9 mm, vias 4 -> 5
- net +3V3: track 214.8 -> 115.8 mm, vias 35 -> 27
- net DISP_D1_FMC: track 156.9 -> 61.8 mm, vias 5 -> 1
- net DISP_D4_FMC: track 152.8 -> 60.7 mm, vias 5 -> 2
- net DISP_D0_FMC: track 159.6 -> 67.7 mm, vias 5 -> 1
- net DISP_D7_FMC: track 144.7 -> 54.6 mm, vias 5 -> 2
- net DISP_D6_FMC: track 146.9 -> 59.2 mm, vias 5 -> 2
- net DISP_D3_FMC: track 147.2 -> 60.2 mm, vias 5 -> 2
- net DISP_CS0: track 2.05 -> 87.6 mm, vias 0 -> 1
- net GND: track 140.6 -> 64.8 mm, vias 53 -> 94
- net DISP_NWE_FMC: track 10.5 -> 83.0 mm, vias 0 -> 1
- net DISP_D2_FMC: track 146.4 -> 75.7 mm, vias 5 -> 1
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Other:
- board size 100 x 76.8 mm -> 105.6 x 76.8 mm
- board text added: "DC IN 10V"
- board text added: "DIGILOG DEV"
- board text added: "DISP_PWM SREG_DAT"
- board text added: "F2_MB F2_MA F0_ADC COMP1_CV F2_TOUCH DISP_CS2 DISP_CS0 F1_MA COMP_ADC0 LED_LAT COMP_ADC3 COMP_ADC1 COMP_CV3"
- board text added: "I2C4_CLK I2C3_CLK I2C2_CLK"
- board text added: "I2C4_DAT I2C3_DAT I2C2_DAT"
- board text added: "SREG_CLK GND"
- board text removed: "CH1"
- board text removed: "CH2"
- board text removed: "CH3"
- board text removed: "CH4"
- board text removed: "LOGIC CVs"
- board text removed: "SPI MASTER"
- board text removed: "ST-LINK"

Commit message: fixed led flickering bug due to waiting for floating disconnnected i2c buses to respond until timeout
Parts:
- moved REF** 57.9 mm to (159.4, 179.1), turned to 0 degrees
- moved JP1 3.13 mm to (170.1, 176.7)
- moved R7 3.13 mm to (170.1, 172.9)
- moved JP2 2.94 mm to (170.1, 160.3)
- moved R8 2.94 mm to (170.1, 156.5)
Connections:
- J2 pad 1: F2_MoB -> COMP_CV3
- J2 pad 16: F1_MoB -> COMP_CV0
- J2 pad 17: COMP_ADC0 -> COMP_CV2
- J2 pad 21: COMP_ADC3 -> xPD8
- J2 pad 22: COMP_CV0 -> xPD9
- J2 pad 23: COMP_ADC1 -> COMP_ADC0
- J2 pad 24: COMP_CV2 -> COMP_ADC1
- J2 pad 25: COMP_CV3 -> COMP_ADC2
- J2 pad 26: COMP_ADC2 -> COMP_ADC3
- J2 pad 4: xPA7 -> F2_MoB
- J2 pad 7: COMP_CV1 -> xPB0
- J2 pad 8: F3_MoB -> COMP_CV1
- J6 pad 22: xPB7 -> F3_MoB
- J6 pad 28: DAC_LDAC1 -> F1_MoB
- J6 pad 29: xPD3 -> DAC_LDAC1
- U1 pad 26: F2_MoB -> COMP_CV3
- U1 pad 29: xPA7 -> F2_MoB
- U1 pad 32: COMP_CV1 -> xPB0
- U1 pad 33: F3_MoB -> COMP_CV1
- U1 pad 50: F1_MoB -> COMP_CV0
- U1 pad 51: COMP_ADC0 -> COMP_CV2
- U1 pad 55: COMP_ADC3 -> xPD8
- U1 pad 56: COMP_CV0 -> xPD9
- U1 pad 57: COMP_ADC1 -> COMP_ADC0
- U1 pad 58: COMP_CV2 -> COMP_ADC1
- U1 pad 59: COMP_CV3 -> COMP_ADC2
- U1 pad 60: COMP_ADC2 -> COMP_ADC3
- U1 pad 85: xPD3 -> DAC_LDAC1
- U1 pad 88: DAC_LDAC1 -> F1_MoB
- U1 pad 94: xPB7 -> F3_MoB
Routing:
- net DISP_RST: track 78.6 -> 192.6 mm, vias 1 -> 7
- net DISP_BL-: track 14.3 -> 88.9 mm
- net DISP_CS3: track 36.8 -> 104.5 mm, vias 0 -> 2
- net DISP_D7_FMC: track 54.6 -> 112.3 mm, vias 2 -> 3
- net DISP_D6_FMC: track 59.2 -> 116.0 mm, vias 2 -> 3
- net DISP_D5_FMC: track 46.8 -> 102.4 mm, vias 2 -> 3
- net DISP_D4_FMC: track 60.7 -> 116.2 mm, vias 2 -> 3
- net SWDIO: track 50.0 -> 105.0 mm, vias 2 -> 3
- net SWDCK: track 47.5 -> 101.4 mm, vias 2 -> 3
- net DISP_A0_FMC: track 72.1 -> 123.9 mm, vias 1 -> 3
- net DISP_CS2: track 39.7 -> 89.0 mm, vias 0 -> 2
- net xPB0: track 0.00 -> 43.3 mm
- net DISP_D0_FMC: track 67.7 -> 110.9 mm, vias 1 -> 4
- net xPD3: track 42.5 -> 0.00 mm, vias 2 -> 0
- net xPA7: track 42.2 -> 0.00 mm
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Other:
- board text added: "** Currently unused pins"
- board text added: "**[PA7]"
- board text added: "**[PB7]"
- board text added: "**[PC14]"
- board text added: "**[PC15]"
- board text added: "**[PD3]"
- board text added: "**[PE0]"
- board text added: "**[PE1]"
- board text added: "**[PE2]"
- board text added: "**[PE3]"
- board text added: "**[PE6]"
- board text added: "**[PF2]"
- board text added: "**[PF9]"
- board text added: "10V"
- board text added: "3.3V"
- board text added: "3V3"
- board text added: "5V"
- board text added: "A0"
- board text added: "DATA0"
- board text added: "DATA1"
- board text added: "DATA2"
- board text added: "DATA3"
- board text added: "DATA4"
- board text added: "DATA5"
- board text added: "DATA6"
- board text added: "DATA7"
- board text added: "DISP DATA"
- board text added: "DISP_PWM"
- board text added: "F2_MB F2_MA F0_ADC COMP1_CV F2_TOUCH DISP2_CS DISP0_CS F1_MA COMP0_ADC COMP3_ADC COMP1_ADC COMP3_CV"
- board text added: "Fo_MA F1_TOUCH F3_MB DISP3_CS DISP1_CS F3_TOUCH F1_MB COMP0_CV COMP2_CV COMP2_ADC"
- board text added: "GND"
- board text added: "I2C1_CLK"
- board text added: "I2C1_DAT"
- board text added: "LED_CLK LED_DAT"
- board text added: "LED_LAT"
- board text added: "LED_PWM"
- board text added: "Lift black latch Contacts facing DOWN Close black latch"
- board text added: "NOE"
- board text added: "NWE"
- board text added: "SREG_CLK"
- board text added: "SREG_DAT"
- board text added: "SREG_LAT"
- board text added: "STLINK-V3"
- board text added: "Skylar. D 2026 Rev 0 RoHS"
- board text added: "UART_RX F0_MB F2_ADC F1_ADC F3_MA MASTER_CS MASTER_MISO DISP_NE1 DAC2_LDAC DAC4_LDAC SWDCK"
- board text added: "UART_TX F3_ADC F0_TOUCH GND MOSI CLOCK DAC1_LDAC DAC0_LDAC DAC3_LDAC SWDIO"
- board text added: "[For probing only]"
- board text removed: "DISP_PWM SREG_DAT"
- board text removed: "F2_MB F2_MA F0_ADC COMP1_CV F2_TOUCH DISP_CS2 DISP_CS0 F1_MA COMP_ADC0 LED_LAT COMP_ADC3 COMP_ADC1 COMP_CV3"
- board text removed: "SREG_CLK GND"

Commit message: dev/maybe final digital logic board. note to self still need to fix crowbar overvolt prot and the pwm disp backlight driver transistor
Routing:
- net DISP_D5_FMC: track 102.4 -> 162.9 mm, vias 3 -> 6
- net DISP_D4_FMC: track 116.2 -> 171.3 mm, vias 3 -> 6
- net DISP_D2_FMC: track 102.7 -> 156.2 mm, vias 2 -> 5
- net DISP_D0_FMC: track 110.9 -> 164.1 mm, vias 4 -> 7
- net DISP_D6_FMC: track 116.0 -> 168.8 mm, vias 3 -> 6
- net DISP_D1_FMC: track 101.9 -> 152.8 mm, vias 4 -> 7
- net DISP_A0_FMC: track 123.9 -> 173.7 mm, vias 3 -> 6
- net DISP_D3_FMC: track 101.8 -> 151.5 mm, vias 3 -> 6
- net DISP_NOE_FMC: track 103.8 -> 153.2 mm, vias 2 -> 5
- net DISP_NWE_FMC: track 109.4 -> 158.5 mm, vias 2 -> 5
- net DISP_D7_FMC: track 112.3 -> 159.9 mm, vias 3 -> 6
- net +3V3: track 113.0 -> 139.0 mm, vias 27 -> 41
- net DISP_RST: track 192.6 -> 217.5 mm, vias 7 -> 8
- net +5V: track 146.1 -> 144.3 mm
- net NRST: track 49.4 -> 48.3 mm
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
